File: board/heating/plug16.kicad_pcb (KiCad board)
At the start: 2 copper layers, 40.7 x 47.4 mm, 16 parts, among them J1 Moat_Bus_16, J10 1wireConn, J2 Moat_Bus_wire, J3 SCLK, J4 SDA, J5 3V3, J6 GND, J8 S1, J9 S2, Q1 2N7002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

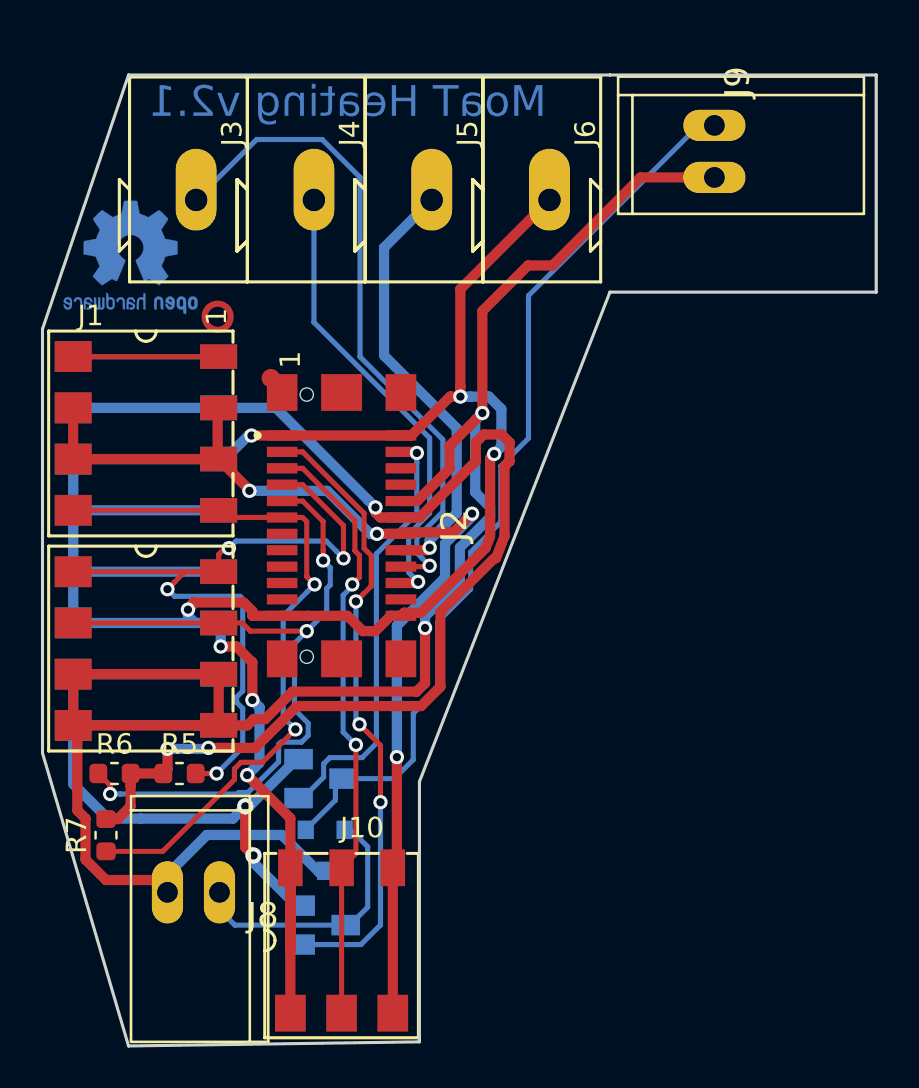
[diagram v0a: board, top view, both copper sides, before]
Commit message: Too many reworks to count.
Most notably: Split GND and GNDPWR.
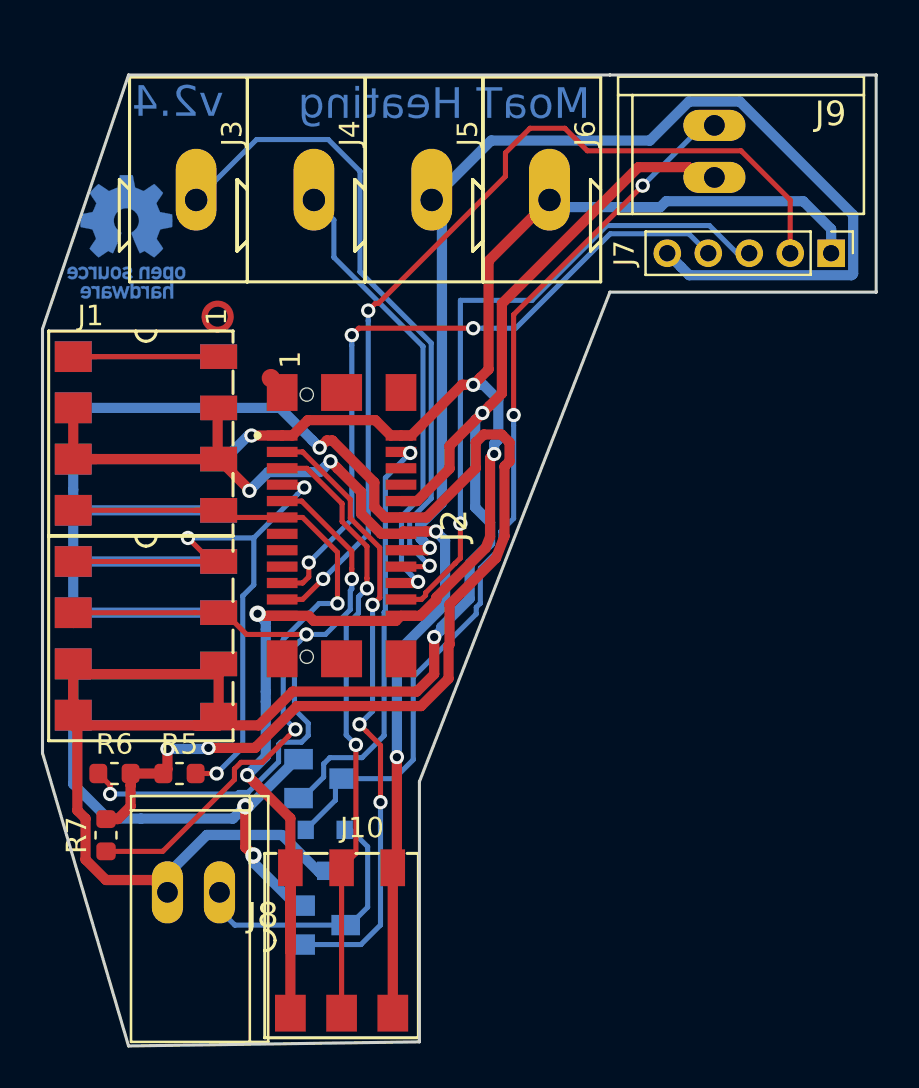
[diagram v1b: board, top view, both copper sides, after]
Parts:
- removed the REF** at (23.6, 38.4)
- added J7: Conn_01x05, Connector_PinHeader_2.00mm:PinHeader_1x05_P2.00mm_Vertical, F.Cu at (57.8, 38.2)
- added REF**: OSHW-Logo_5.7x6mm_Copper, Symbol:OSHW-Logo_5.7x6mm_Copper, B.Cu at (23.4, 37.4)
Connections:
- net Net-(D1-Pad3) renamed +24V
- net Net-(J1-Pad10) renamed GND
- net Net-(J1-Pad3) renamed +5V
- net Net-(J1-Pad4) renamed +12V
- J2 pad 13: Net-(J2-Pad13) -> (no net)
- J2 pad 15: Net-(J2-Pad15) -> (no net)
- J2 pad 17: Net-(J2-Pad17) -> (no net)
- J2 pad 6: Net-(J2-Pad6) -> (no net)
- J2 pad 8: Net-(J2-Pad8) -> (no net)
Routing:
- net Net-(J2-Pad21): track 0.00 -> 45.4 mm, vias 0 -> 2
- net Net-(J2-Pad16): track 21.4 -> 56.5 mm
- net Net-(J2-Pad19): track 0.00 -> 33.9 mm, vias 0 -> 3
- net Net-(J2-Pad22): track 0.00 -> 32.6 mm, vias 0 -> 1
- net GND: track 113.5 -> 124.0 mm, vias 7 -> 5
- net Net-(J1-Pad9): track 38.0 -> 30.2 mm, vias 4 -> 3
- net Net-(J1-Pad11): track 38.2 -> 39.8 mm
- net +5V: track 53.6 -> 52.1 mm
- net Net-(J1-Pad7): track 36.0 -> 37.4 mm
- net +12V: track 59.8 -> 60.8 mm
- net Net-(D1-Pad1): track 44.5 -> 44.4 mm, vias 0 -> 2
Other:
- board text added: "MoaT Heating"
- board text added: "v2.4"
- board text removed: "MoaT Heating v2.1"
